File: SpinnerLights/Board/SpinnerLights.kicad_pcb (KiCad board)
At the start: 2 copper layers, 78 x 74.1 mm, 14 parts, among them U1 SeeeduinoXIAO, U2 ADXL343

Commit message: SpinnerLights: move a couple of components around to give more space
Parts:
- moved U2 0.82 mm to (113.0, 72.3)
- moved R2 0.40 mm to (117.8, 68.4)
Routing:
- net SDA: track 32.3 -> 30.0 mm
- net INT2: track 10.2 -> 11.7 mm
- net SCL: track 29.8 -> 30.7 mm

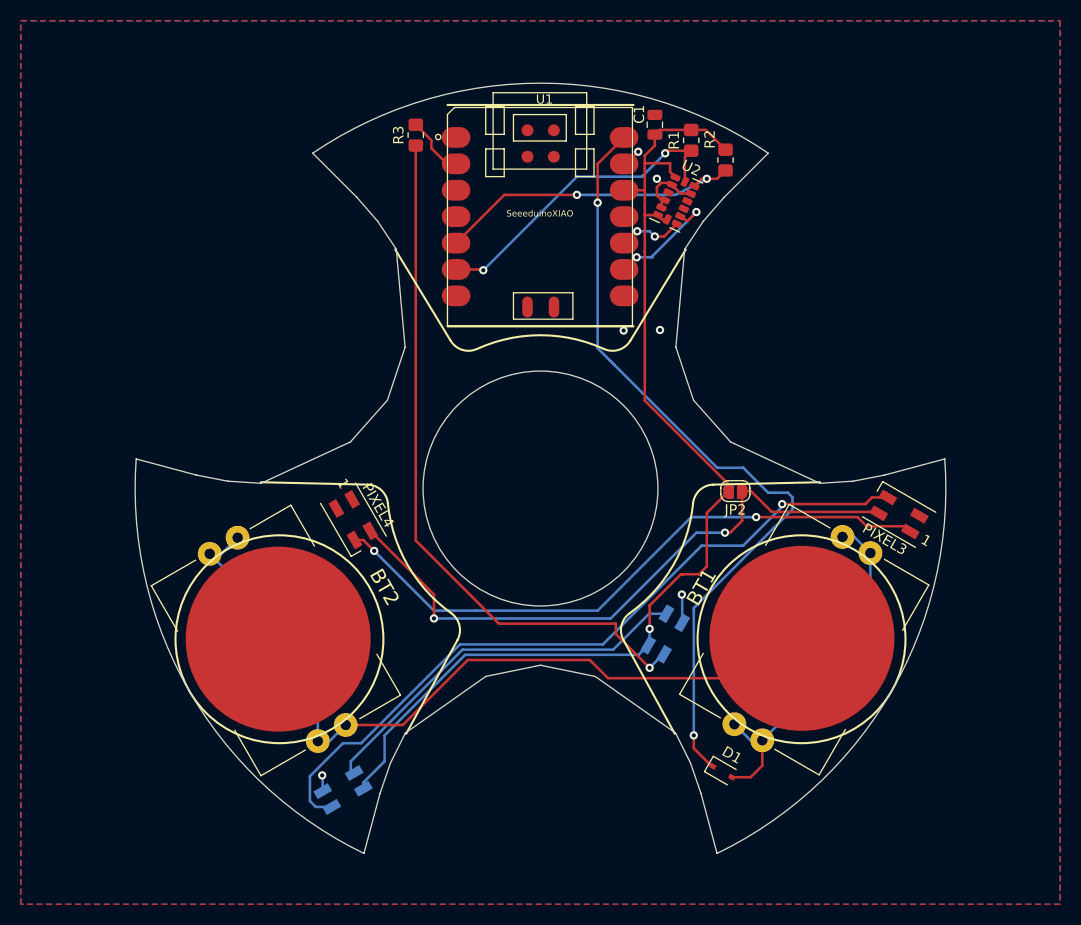
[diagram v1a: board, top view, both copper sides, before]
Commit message: SpinnerLights: Minor tweaks to placement and routing
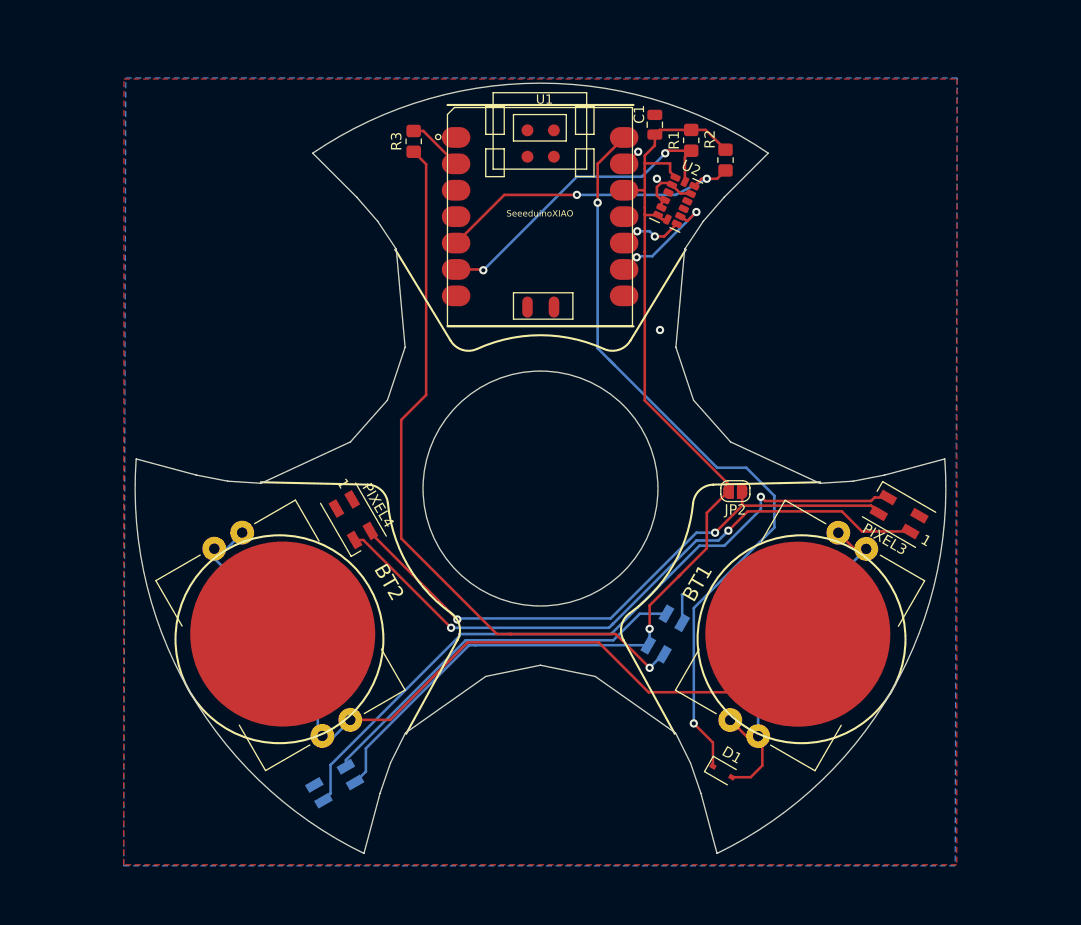
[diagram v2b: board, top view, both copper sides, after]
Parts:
- moved PIXEL2 1.00 mm to (80.2, 128.4)
- moved BT2 0.66 mm to (75.2, 114.0)
- moved R3 0.63 mm to (87.8, 66.6)
- moved BT1 0.57 mm to (124.8, 114.0)
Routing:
- net /B15: track 77.8 -> 74.2 mm
- net Net-(BT1-PadP1): track 34.8 -> 38.2 mm
- net Net-(JP2-Pad1): track 61.5 -> 58.9 mm
- net Net-(D1-Pad1): track 77.6 -> 75.1 mm
- net Net-(PIXEL3-Pad1): track 60.6 -> 62.7 mm
- net Net-(PIXEL2-Pad1): track 71.8 -> 69.9 mm
- net Net-(Pixel1-Pad3): track 68.5 -> 70.3 mm
- net GND: track 14.1 -> 12.6 mm, vias 6 -> 3
- net +3V3: track 108.2 -> 107.6 mm
